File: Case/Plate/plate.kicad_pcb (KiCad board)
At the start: 2 copper layers, 139.1 x 77.2 mm, 4 parts

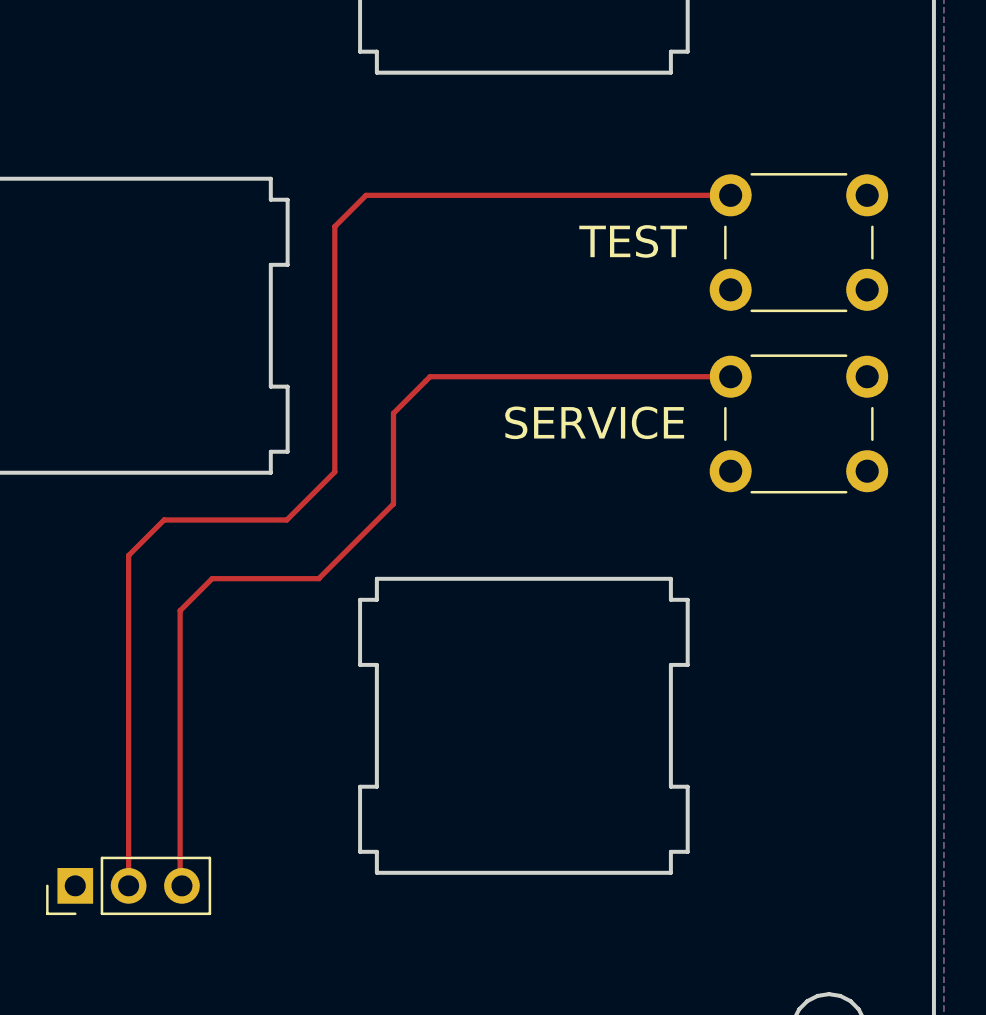
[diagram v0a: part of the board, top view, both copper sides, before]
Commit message: Use 90 degree buttons for test/service, smol fixes
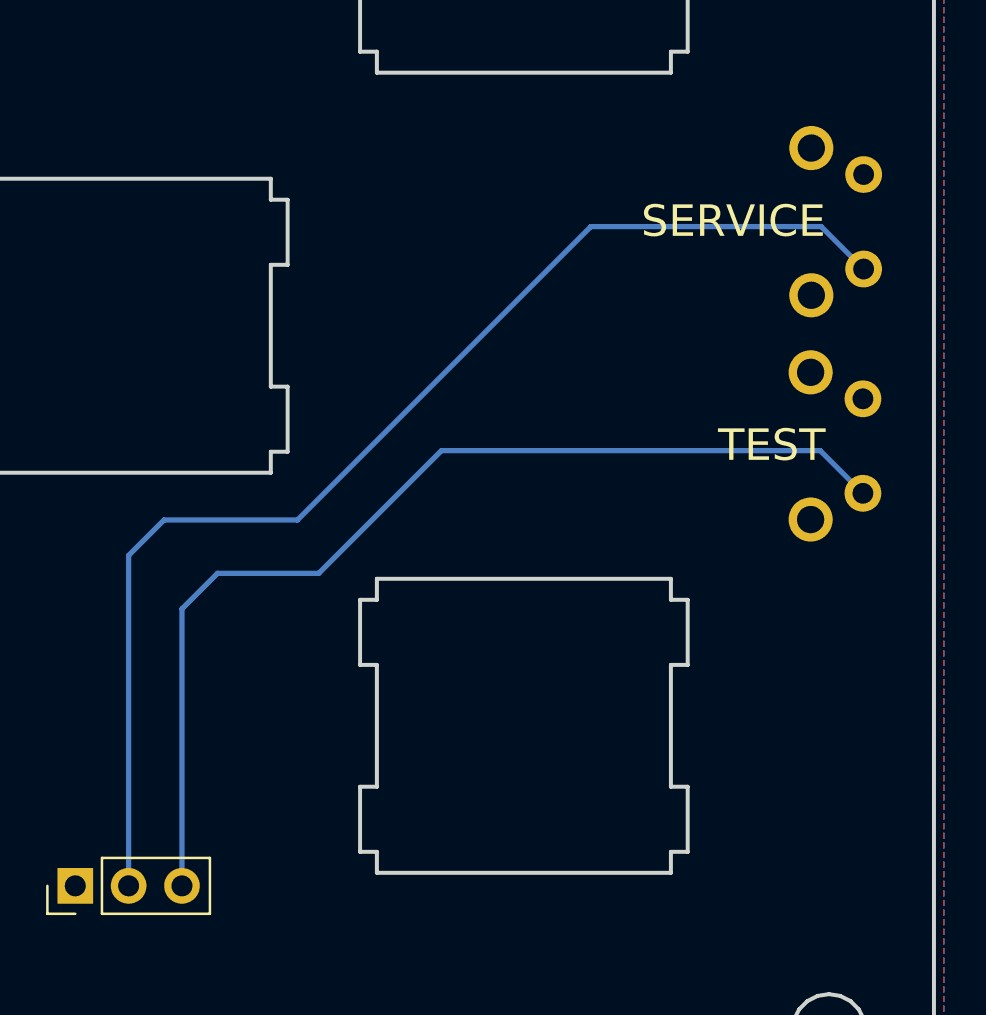
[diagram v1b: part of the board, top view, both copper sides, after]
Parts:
- removed the REF** at (209.9, 100.4)
- removed the REF** at (209.9, 91.7)
- added REF**: SW_Tactile_SPST_Angled_PTS645Vx39-2LFS, Button_Switch_THT:SW_Tactile_SPST_Angled_PTS645Vx39-2LFS, B.Cu at (216.2, 95.2)
- added REF**: SW_Tactile_SPST_Angled_PTS645Vx39-2LFS, Button_Switch_THT:SW_Tactile_SPST_Angled_PTS645Vx39-2LFS, B.Cu at (216.2, 105.9)
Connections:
- REF** pad 2: TEST -> SERVICE
- REF** pad 3: SERVICE -> TEST
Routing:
- net SERVICE: track 46.5 -> 58.1 mm
- net TEST: track 58.3 -> 49.6 mm

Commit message: Final PCB changes for now. See description
Not making even a single change to either PCB until I receive the initial batch and thoroughly test everything. If any changes need to be made, they'll be made then. README and such will continue to be updated, though.
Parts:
- added G***: LOGO, LogoFootprints:Arrow_6, B.Cu at (207.8, 131.6)
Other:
- board text added: "PicoFX Plate Rev. 1 https://github.com/dj505/PicoFX"
